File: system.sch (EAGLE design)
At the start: 64 parts, among them IC1 TPS7B8650BQDDARQ1, IC2 TLV9101IDBVR, IC3 TLV9101IDBVR, J1 TSW-104-07-F-S, J2 163-179PH-EX, J3 RS1-02-G, SW1 1825910-6, SW2 1825910-6, SW3 1825910-6, U1 ATMEGA328PB-AU

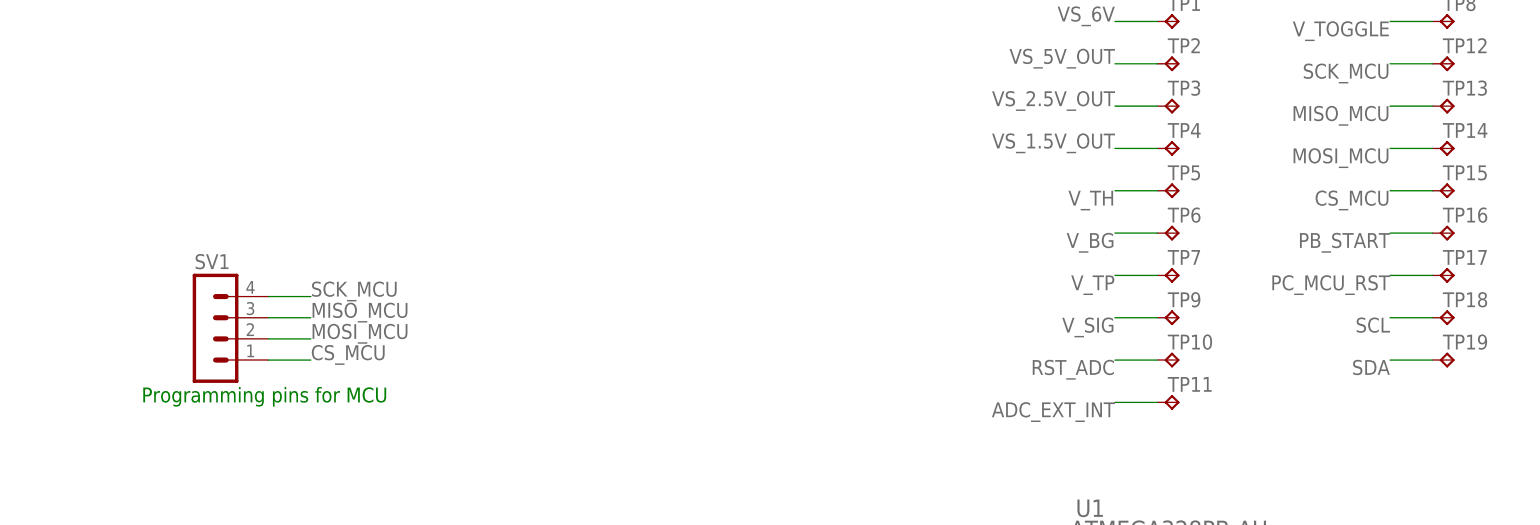
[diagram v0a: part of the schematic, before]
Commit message: fixed warnings
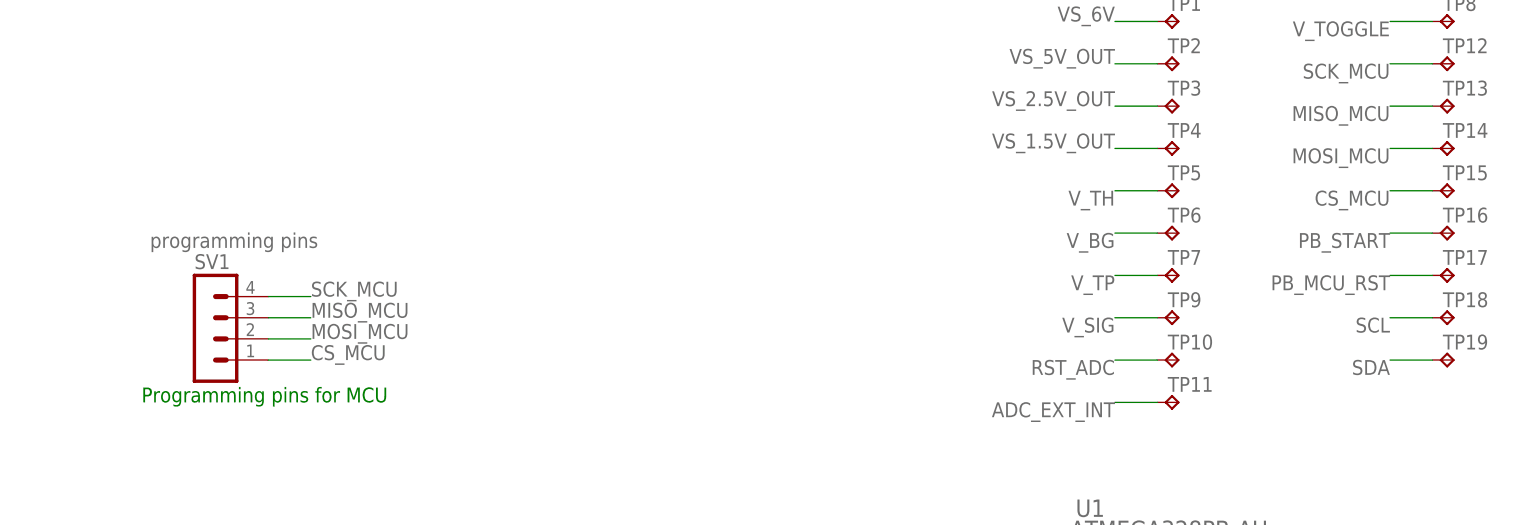
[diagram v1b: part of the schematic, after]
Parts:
- SV1: value (none) -> programming pins
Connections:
- removed net N$12: U1.(ICP1/CLKO/PTCXY)PB0
- removed net N$13: U1.(OC1A/PTCXY)PB1
- removed net PC_MCU_RST: TP17.TP
- net PB_MCU_RST: now also TP17.TP
- net PB_MISC1: now also U1.(OC1A/PTCXY)PB1
- net PB_START: now also U1.(ICP1/CLKO/PTCXY)PB0
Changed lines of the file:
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@@
 <part name="R24" library="rcl" library_urn="urn:adsk.eagle:library:334" deviceset="R-US_" device="R0603" package3d_urn="urn:adsk.eagle:package:23555/3" value="20000"/>
 <part name="C8" library="rcl" library_urn="urn:adsk.eagle:library:334" deviceset="C-US" device="C0603" package3d_urn="urn:adsk.eagle:package:23616/2" value="10uF"/>
-<part name="SV1" library="con-lstb" library_urn="urn:adsk.eagle:library:162" deviceset="MA04-1" device="" package3d_urn="urn:adsk.eagle:package:8337/1"/>
+<part name="SV1" library="con-lstb" library_urn="urn:adsk.eagle:library:162" deviceset="MA04-1" device="" package3d_urn="urn:adsk.eagle:package:8337/1" value="programming pins"/>
 <part name="TP1" library="testpad" library_urn="urn:adsk.eagle:library:385" deviceset="TP" device="PAD1-13" package3d_urn="urn:adsk.eagle:package:27946/1"/>
 <part name="TP2" library="testpad" library_urn="urn:adsk.eagle:library:385" deviceset="TP" device="PAD1-13" package3d_urn="urn:adsk.eagle:package:27946/1"/>
@@
 </instance>
 <instance part="SV1" gate="1" x="-317.5" y="-33.02" smashed="yes">
-<attribute name="VALUE" x="-318.77" y="-43.18" size="1.778" layer="96"/>
+<attribute name="VALUE" x="-324.104" y="-24.638" size="1.778" layer="96"/>
 <attribute name="NAME" x="-318.77" y="-27.178" size="1.778" layer="95"/>
 </instance>
@@
 <label x="-137.16" y="-73.66" size="1.778" layer="95"/>
 </segment>
+<segment>
+<pinref part="TP17" gate="G$1" pin="TP"/>
+<wire x1="-170.18" y1="-27.94" x2="-175.26" y2="-27.94" width="0.1524" layer="91"/>
+<label x="-175.26" y="-27.94" size="1.778" layer="95" rot="R180"/>
+</segment>
 </net>
 <net name="PB_START" class="0">
@@
 <wire x1="-304.8" y1="-101.6" x2="-299.72" y2="-101.6" width="0.1524" layer="91"/>
 <label x="-297.18" y="-111.76" size="1.778" layer="95"/>
-<label x="-274.32" y="-93.98" size="1.778" layer="95" align="bottom-right"/>
 <wire x1="-299.72" y1="-101.6" x2="-299.72" y2="-111.76" width="0.1524" layer="91"/>
 <wire x1="-299.72" y1="-111.76" x2="-297.18" y2="-111.76" width="0.1524" layer="91"/>
@@
 <label x="-175.26" y="-22.86" size="1.778" layer="95" rot="R180"/>
 </segment>
-</net>
-<net name="N$12" class="0">
 <segment>
 <pinref part="U1" gate="A" pin="(ICP1/CLKO/PTCXY)PB0"/>
 <wire x1="-271.78" y1="-93.98" x2="-274.32" y2="-93.98" width="0.1524" layer="91"/>
-</segment>
-</net>
-<net name="PB_MISC1" class="0">
-<segment>
-<pinref part="SW2" gate="G$1" pin="3"/>
-<wire x1="-304.8" y1="-119.38" x2="-297.18" y2="-119.38" width="0.1524" layer="91"/>
-<label x="-297.18" y="-119.38" size="1.778" layer="95"/>
-<label x="-274.32" y="-96.52" size="1.778" layer="95" align="bottom-right"/>
-</segment>
-</net>
-<net name="N$13" class="0">
-<segment>
-<pinref part="U1" gate="A" pin="(OC1A/PTCXY)PB1"/>
-<wire x1="-271.78" y1="-96.52" x2="-274.32" y2="-96.52" width="0.1524" layer="91"/>
+<label x="-274.32" y="-93.98" size="1.778" layer="95" align="bottom-right"/>
 </segment>
 </net>
@@
 </segment>
 </net>
-<net name="PC_MCU_RST" class="0">
-<segment>
-<pinref part="TP17" gate="G$1" pin="TP"/>
-<wire x1="-170.18" y1="-27.94" x2="-175.26" y2="-27.94" width="0.1524" layer="91"/>
-<label x="-175.26" y="-27.94" size="1.778" layer="95" rot="R180"/>
-</segment>
-</net>
+<net name="PB_MISC1" class="0">
+<segment>
+<pinref part="SW2" gate="G$1" pin="3"/>
+<wire x1="-304.8" y1="-119.38" x2="-297.18" y2="-119.38" width="0.1524" layer="91"/>
+<label x="-297.18" y="-119.38" size="1.778" layer="95"/>
+</segment>
+<segment>
+<pinref part="U1" gate="A" pin="(OC1A/PTCXY)PB1"/>
+<wire x1="-271.78" y1="-96.52" x2="-274.32" y2="-96.52" width="0.1524" layer="91"/>
+<label x="-274.32" y="-96.52" size="1.778" layer="95" align="bottom-right"/>
+</segment>
+</net>

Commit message: added cap to 2.5V reference
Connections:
- new net GND: C1.2, C2.2, C3.2, C4.2, C5.2, C6.2, C7.2, C8.2, IC1.-VS, IC1.EP, IC1.GND, IC1.V-, IC2.THERMISTOR_GND, IC2.V-, IC3.V-, J1.01, J1.2, J2.B, J2.C, J3.1, R2.1, R21.1, R4.1, R6.1, R8.1, SW1.1, SW2.1, SW3.1, U1.GND, U1.GND_2
- net 0: no longer C1.2, C2.2, C3.2, C4.2, C6.2, C7.2, C8.2, IC1.-VS, IC1.EP, IC1.GND, IC1.V-, IC2.THERMISTOR_GND, IC2.V-, IC3.V-, J1.01, J1.2, J2.B, J2.C, J3.1, R2.1, R21.1, R4.1, R6.1, R8.1, SW1.1, SW2.1, SW3.1, U1.GND, U1.GND_2
- net VS_2.5V: now also C5.1
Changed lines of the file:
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@@
 </segment>
 </net>
-<net name="0" class="0">
+<net name="GND" class="0">
 <segment>
 <pinref part="IC1" gate="G$1" pin="EP"/>
@@
 <wire x1="111.76" y1="33.02" x2="106.68" y2="33.02" width="0.1524" layer="91"/>
 <junction x="106.68" y="33.02"/>
+<label x="111.76" y="33.02" size="1.778" layer="95"/>
 </segment>
 </net>
@@
 <part name="R7" library="rcl" library_urn="urn:adsk.eagle:library:334" deviceset="R-US_" device="R0603" package3d_urn="urn:adsk.eagle:package:23555/3" value="0"/>
 <part name="R8" library="rcl" library_urn="urn:adsk.eagle:library:334" deviceset="R-US_" device="R0603" package3d_urn="urn:adsk.eagle:package:23555/3" value="0"/>
+<part name="C5" library="rcl" library_urn="urn:adsk.eagle:library:334" deviceset="C-US" device="C0603" package3d_urn="urn:adsk.eagle:package:23616/2" value="1uF"/>
+<part name="X_7" library="ngspice-simulation" library_urn="urn:adsk.eagle:library:527439" deviceset="GND" device=""/>
 </parts>
 <sheets>
@@
 <attribute name="VALUE" x="2.794" y="27.178" size="1.778" layer="96"/>
 </instance>
+<instance part="C5" gate="G$1" x="106.68" y="60.96" smashed="yes">
+<attribute name="NAME" x="107.696" y="61.595" size="1.778" layer="95"/>
+<attribute name="VALUE" x="107.696" y="56.769" size="1.778" layer="96"/>
+</instance>
+<instance part="X_7" gate="G$1" x="106.68" y="50.8" smashed="yes"/>
 </instances>
 <busses>
 </busses>
 <nets>
-<net name="0" class="0">
+<net name="GND" class="0">
 <segment>
 <wire x1="-73.66" y1="76.2" x2="-78.74" y2="76.2" width="0.1524" layer="91"/>
@@
 <pinref part="X_9" gate="G$1" pin="0"/>
 <wire x1="-2.54" y1="27.94" x2="-2.54" y2="22.86" width="0.1524" layer="91"/>
+<label x="-2.54" y="22.86" size="1.778" layer="95"/>
 </segment>
 <segment>
@@
 <pinref part="IC2" gate="G$1" pin="IN-"/>
 <wire x1="104.14" y1="68.58" x2="101.6" y2="68.58" width="0.1524" layer="91"/>
-<wire x1="104.14" y1="68.58" x2="109.22" y2="68.58" width="0.1524" layer="91"/>
+<wire x1="104.14" y1="68.58" x2="106.68" y2="68.58" width="0.1524" layer="91"/>
 <junction x="104.14" y="68.58"/>
 <label x="109.22" y="68.58" size="1.778" layer="95"/>
+<pinref part="C5" gate="G$1" pin="1"/>
+<wire x1="106.68" y1="68.58" x2="109.22" y2="68.58" width="0.1524" layer="91"/>
+<wire x1="106.68" y1="63.5" x2="106.68" y2="68.58" width="0.1524" layer="91"/>
+<junction x="106.68" y="68.58"/>
 </segment>
 <segment>
@@
 <junction x="-22.86" y="55.88"/>
 <pinref part="C4" gate="G$1" pin="1"/>
+</segment>
+</net>
+<net name="0" class="0">
+<segment>
+<pinref part="C5" gate="G$1" pin="2"/>
+<wire x1="106.68" y1="55.88" x2="106.68" y2="50.8" width="0.1524" layer="91"/>
+<pinref part="X_7" gate="G$1" pin="0"/>
 </segment>
 </net>
@@
 </segment>
 </net>
-<net name="0" class="0">
+<net name="GND" class="0">
 <segment>
 <pinref part="Q1" gate="G$1" pin="E3"/>
@@
 <wire x1="55.88" y1="7.62" x2="55.88" y2="2.54" width="0.1524" layer="91"/>
 <junction x="55.88" y="2.54"/>
+<label x="55.88" y="2.54" size="1.778" layer="95"/>
 </segment>
 <segment>
@@
 </busses>
 <nets>
-<net name="0" class="0">
+<net name="GND" class="0">
 <segment>
 <pinref part="IC2" gate="G$1" pin="THERMISTOR_GND"/>
@@
 <wire x1="-15.24" y1="25.4" x2="-15.24" y2="20.32" width="0.1524" layer="91"/>
 <pinref part="X_1" gate="G$1" pin="0"/>
+<label x="-15.24" y="20.32" size="1.778" layer="95"/>
 </segment>
 </net>
@@
 </busses>
 <nets>
-<net name="0" class="0">
+<net name="GND" class="0">
 <segment>
 <pinref part="IC1" gate="G$1" pin="-VS"/>
@@
 <wire x1="43.18" y1="48.26" x2="43.18" y2="38.1" width="0.1524" layer="91"/>
 <pinref part="X_1" gate="G$1" pin="0"/>
+<label x="43.18" y="38.1" size="1.778" layer="95"/>
 </segment>
 <segment>
@@
 </segment>
 </net>
-<net name="0" class="0">
+<net name="GND" class="0">
 <segment>
 <pinref part="IC1" gate="G$1" pin="V-"/>
@@
 <wire x1="-40.64" y1="-17.78" x2="-40.64" y2="-20.32" width="0.1524" layer="91"/>
 <pinref part="X_6" gate="G$1" pin="0"/>
+<label x="-40.64" y="-20.32" size="1.778" layer="95"/>
 </segment>
 <segment>
@@
 </busses>
 <nets>
-<net name="0" class="0">
+<net name="GND" class="0">
 <segment>
 <pinref part="J2" gate="G$1" pin="C"/>
@@
 <wire x1="-167.64" y1="40.64" x2="-167.64" y2="35.56" width="0.1524" layer="91"/>
 <pinref part="X_18" gate="G$1" pin="0"/>
-</segment>
-<segment>
+<label x="-167.64" y="38.1" size="1.778" layer="95"/>
+</segment>
+<segment>

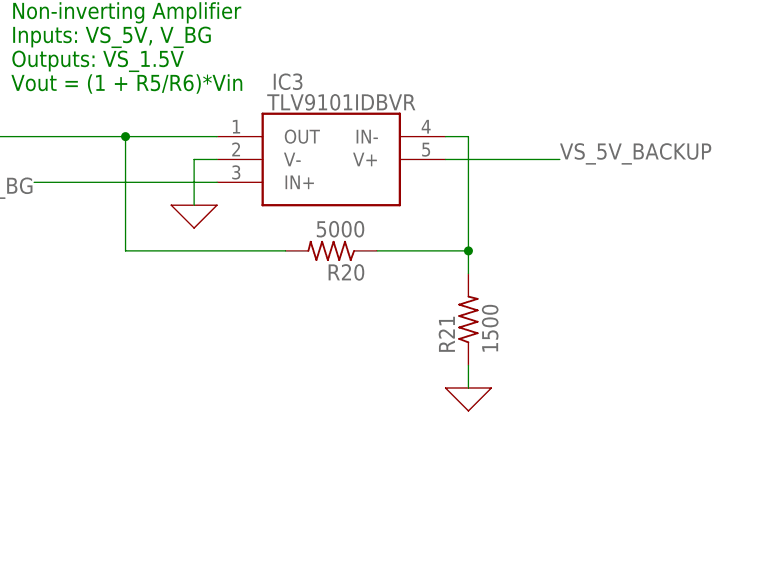
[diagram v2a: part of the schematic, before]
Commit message: connected grounds. added bypass caps to therm/thermopile + amp&filter
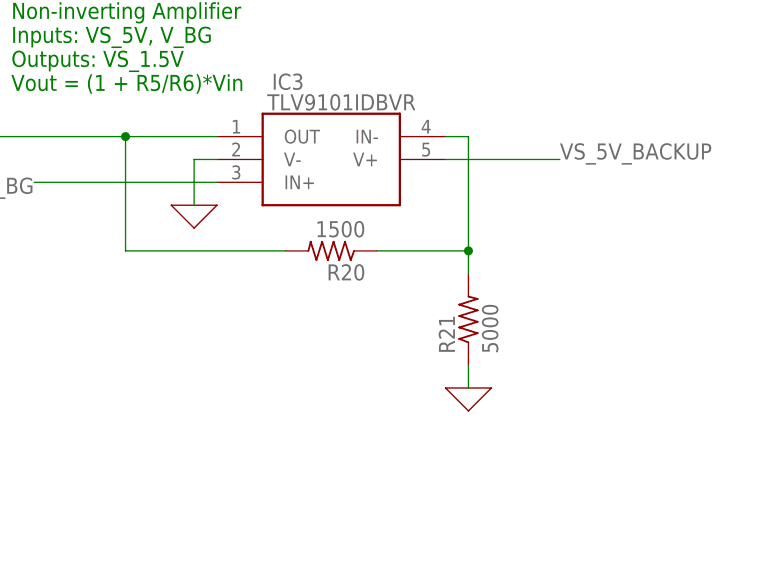
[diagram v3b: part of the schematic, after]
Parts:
- R20: value 5000 -> 1500
- R21: value 1500 -> 5000
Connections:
- net 0: now also C1.2, C2.2, C3.2, IC3.V-
- net N$6: now also IC3.IN+, R5.2
- net VS_1.5V: now also IC3.IN-, IC3.OUT; no longer R5.2
- net VS_2.5V_OUT: now also C2.1, C3.1
- net VS_5V: now also IC3.V+, R5.1
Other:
- note added: "Level Shifter 2 Inputs: VS_5V Outputs: VS_1.5V"

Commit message: Fixed grounds issue
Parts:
- removed TP12, TP15, TP18: TPPAD1-13, testpad:TPPAD1-13
- R24: value 20000 -> 100000
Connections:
- removed net CS_MCU: SV1.1, TP15.TP, U1.(!SS0/OC1B/PTCXY)PB2
- removed net GND: C1.2, C2.2, C3.2, C4.2, C5.2, C6.2, C7.2, C8.2, IC1.-VS, IC1.EP, IC1.GND, IC1.V-, IC2.THERMISTOR_GND, IC2.V-, IC3.V-, J1.01, J1.2, J2.B, J2.C, J3.1, R2.1, R21.1, R4.1, R6.1, R8.1, SW1.1, SW2.1, SW3.1, U1.GND, U1.GND_2
- removed net PB_MCU_RST: SW3.3, TP17.TP, U1.(!RESET)PC6
- new net MCU_RST: SV1.1, SW3.3, TP17.TP, U1.(!RESET)PC6
- net 0: now also C4.2, C6.2, C7.2, C8.2, IC1.-VS, IC1.EP, IC1.GND, IC1.V-, IC2.THERMISTOR_GND, IC2.V-, J1.01, J1.2, J2.B, J2.C, J3.1, R2.1, R21.1, R4.1, R6.1, R8.1, SW1.1, SW2.1, SW3.1, U1.GND, U1.GND_2
- net SCK_MCU: no longer TP12.TP
- net SCL: no longer TP18.TP
